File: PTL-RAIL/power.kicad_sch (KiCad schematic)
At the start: 0 parts

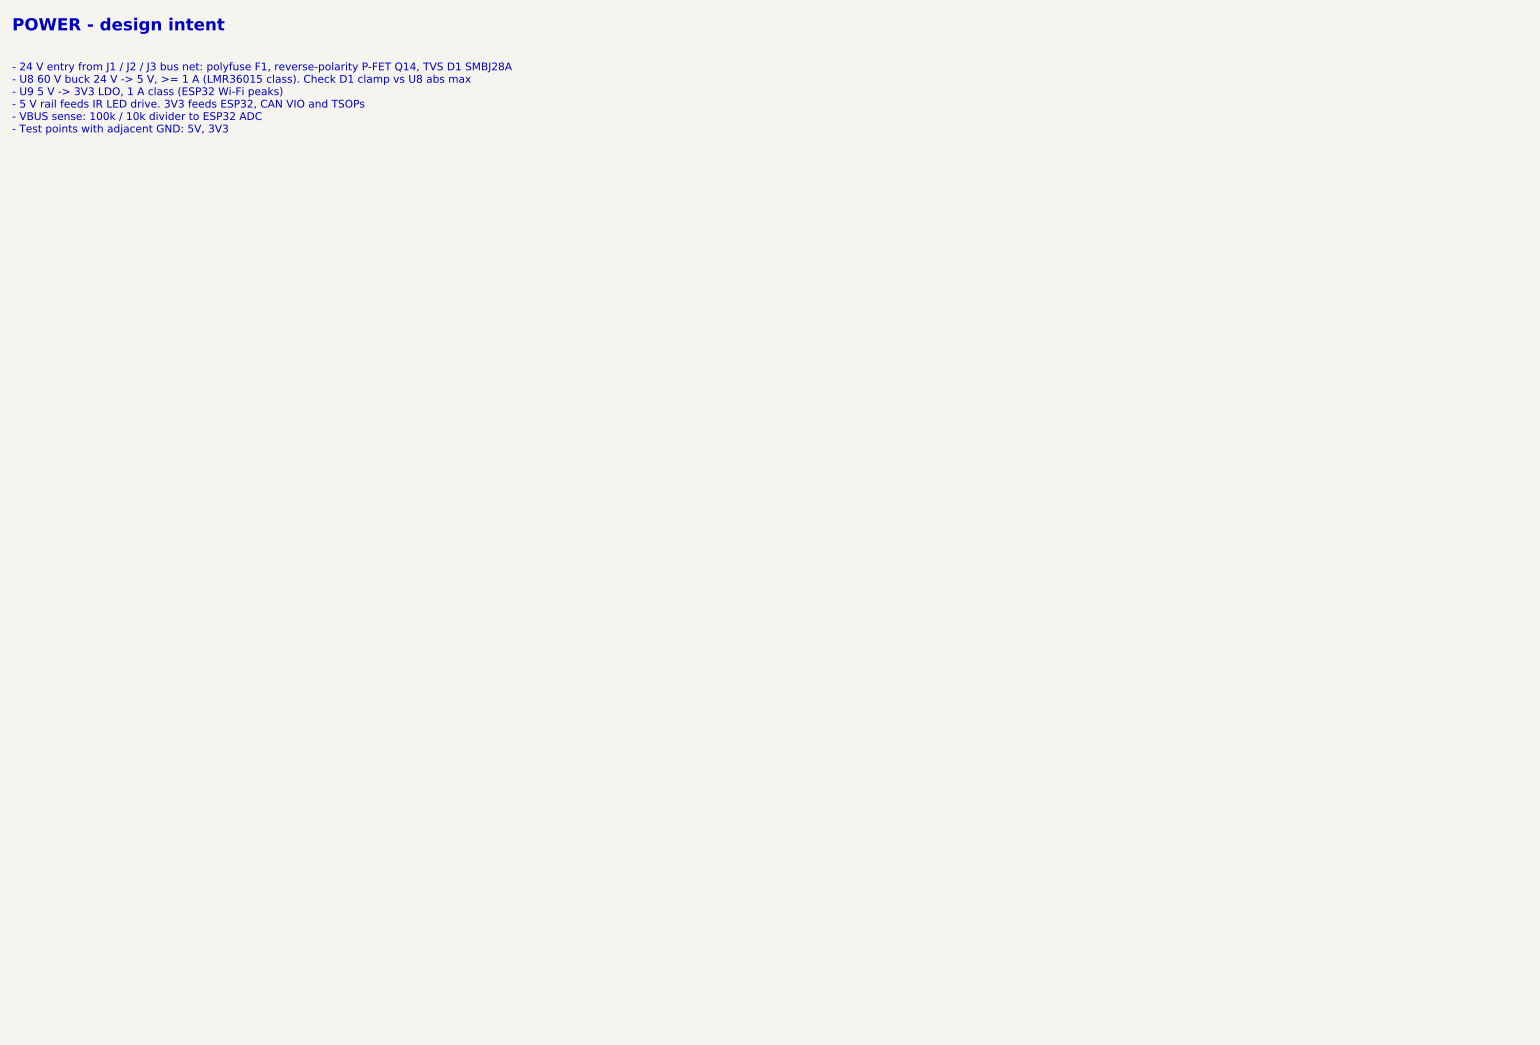
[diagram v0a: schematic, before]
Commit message: PTL-RAIL: LED row on top edge, TSOP row on bottom edge, node parts aligned at 84 mm pitch; J3/J4 10-way and J5/J6 4-way screw terminals
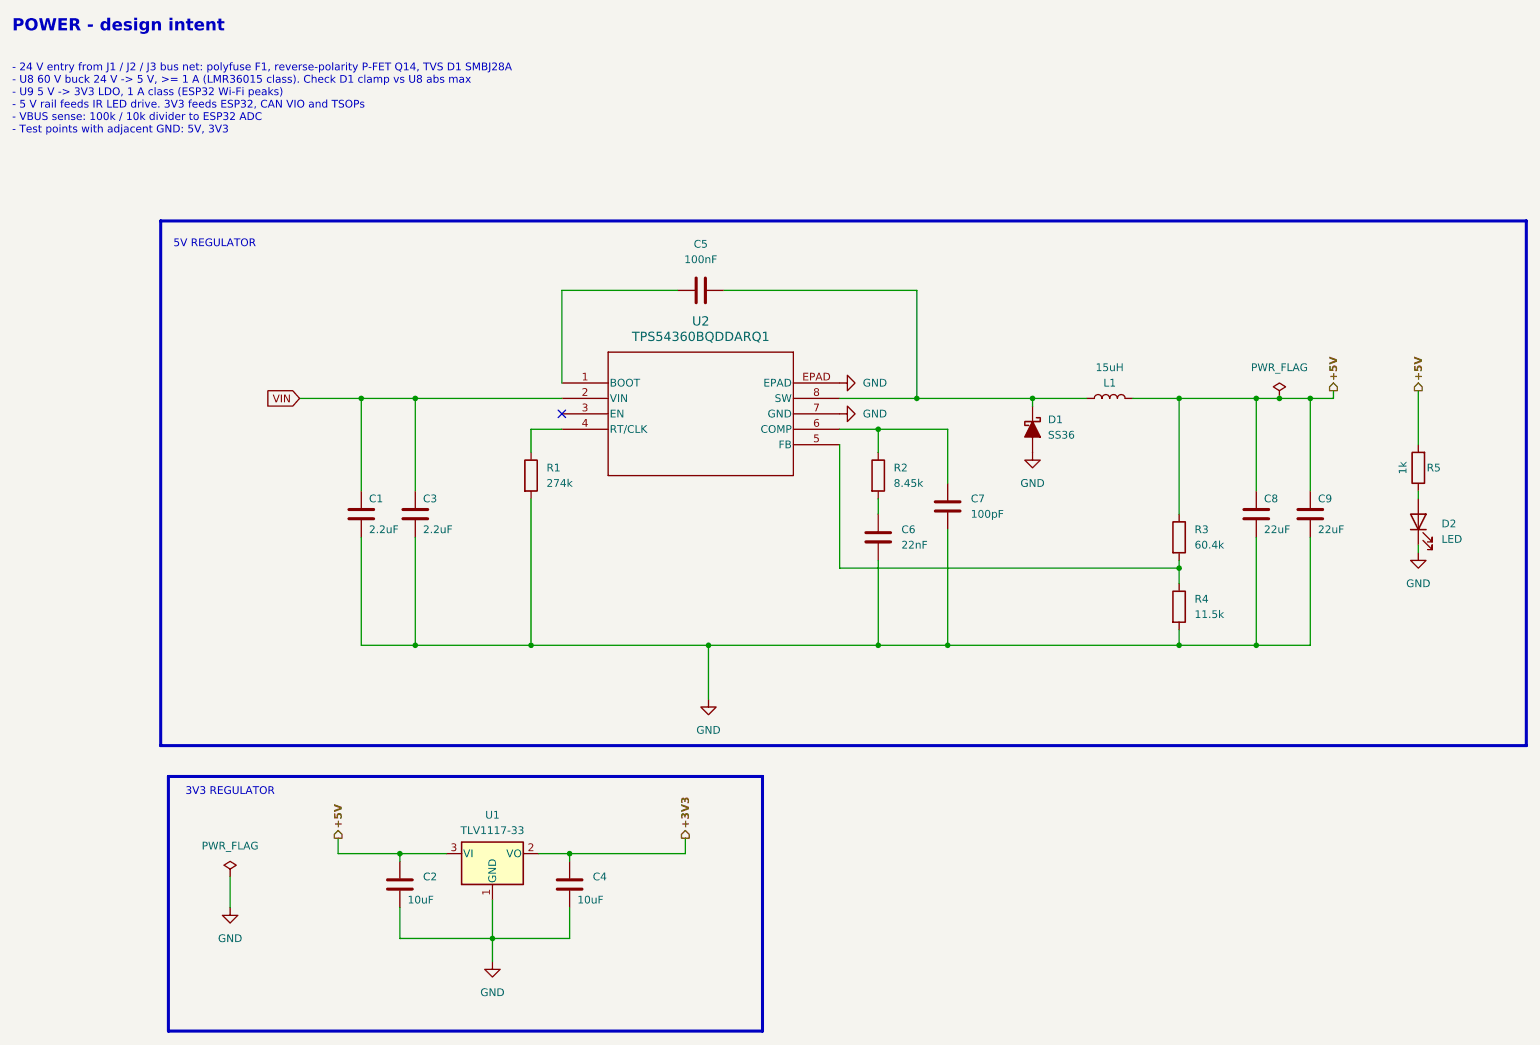
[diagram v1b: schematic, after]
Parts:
- added C1, C3: 2.2uF, Capacitor_SMD:C_1210_3225Metric, symbol Device:C
- added C2, C4: 10uF, Capacitor_SMD:C_0805_2012Metric, symbol Device:C
- added C5: 100nF, Capacitor_SMD:C_0805_2012Metric, symbol Device:C
- added C6: 22nF, Capacitor_SMD:C_0805_2012Metric, symbol Device:C
- added C7: 100pF, Capacitor_SMD:C_0805_2012Metric, symbol Device:C
- added C8, C9: 22uF, Capacitor_SMD:C_1210_3225Metric, symbol Device:C
- added D1: SS36, Diode_SMD:D_SMC, symbol Device:D_Schottky_Filled
- added D2: LED, LED_SMD:LED_0805_2012Metric, symbol Device:LED
- added L1: 15uH, Inductor_SMD:L_APV_ANR8040, symbol Device:L
- added R1: 274k, Resistor_SMD:R_0805_2012Metric, symbol Device:R
- added R2: 8.45k, Resistor_SMD:R_0805_2012Metric, symbol Device:R
- added R3: 60.4k, Resistor_SMD:R_0805_2012Metric, symbol Device:R
- added R4: 11.5k, Resistor_SMD:R_0805_2012Metric, symbol Device:R
- added R5: 1k, Resistor_SMD:R_0805_2012Metric, symbol Device:R
- added U1: TLV1117-33, Package_TO_SOT_SMD:SOT-223-3_TabPin2, symbol Regulator_Linear:TLV1117-33
- added U2: TPS54360BQDDARQ1, 0_IC:TPS54360BQDDARQ1, symbol 0_TPS54360BQDDARQ1:TPS54360BQDDARQ1
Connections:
- new net: R3.2, R4.1, U2.5 (FB)
- new net: C5.2, D1.1 (K), L1.1, U2.8 (SW)
- new net: C5.1, U2.1 (BOOT)
- new net: R1.1, U2.4 (RT/CLK)
- new net: C7.1, R2.1, U2.6 (COMP)
- new net: C6.1, R2.2
- new net: D2.2 (A), R5.1
- new net +3V3: C4.1, U1.2 (VO)
- new net +5V: C2.1, C8.1, C9.1, L1.2, R3.1, R5.2, U1.3 (VI)
- new net GND: C1.2, C2.2, C3.2, C4.2, C6.2, C7.2, C8.2, C9.2, D1.2 (A), D2.1 (K), R1.2, R4.2, U1.1 (GND), U2.7 (GND), U2.EPAD
- new net VIN: C1.1, C3.1, U2.2 (VIN)
- no-connect marks 0 -> 1
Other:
- note added: "3V3 REGULATOR"
- note added: "5V REGULATOR"
